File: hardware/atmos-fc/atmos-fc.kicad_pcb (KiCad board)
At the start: 4 copper layers, 40 x 40 mm, 109 parts, among them J1 Conn_01x04, J2 JST-SH 8p, J3 USB_C_Receptacle_USB2.0_16P, J4 Conn_01x03, J5 Conn_01x06, J6 Conn_01x06, J7 Conn_01x02, Q1 BC817, SW1 SW_Push, U1 MAX25232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

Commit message: Initial commit
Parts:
- removed the G*** at (146.1, 111.3)
- added G***: LOGO, 0_logo:atmos-fc_arrow-logo, F.Cu at (146.0, 111.2)
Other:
- board text removed: "V0.1 | 01/2024"

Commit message: Improved layout
Added oversized holes for mounting silicone inserts and improved layout.
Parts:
- H1, H2, H3, H4: footprint MountingHole:MountingHole_3.2mm_M3 -> MountingHole:MountingHole_4.3mm_M4
- U5: value IIM42352 -> ICM-42688-P
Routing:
- net +BATT_P: track 132.3 -> 147.4 mm, vias 11 -> 14
- net +5V: track 188.4 -> 200.4 mm, vias 23 -> 32
- net /Connectors/BUZZER-: track 7.29 -> 11.5 mm
- net +3V3: track 193.9 -> 192.4 mm
- net /Connectors/UART4_RX_C: track 38.0 -> 37.4 mm
- net /Connectors/UART4_TX_C: track 37.9 -> 37.4 mm
- net /Connectors/I2C_SCK: track 24.6 -> 24.1 mm
- net /Connectors/+5V_USB: track 63.2 -> 62.7 mm
- net GND: vias 135 -> 148

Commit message: Add GYRO_1_EXTI Pin
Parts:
- moved R5 0.50 mm to (141.6, 108.7)
- moved R11 0.30 mm to (137.5, 108.7)
- moved R4 0.25 mm to (140.2, 108.7)
- moved R17 0.20 mm to (135.6, 108.9)
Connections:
- net /MCU/BUZZER_CTRL renamed /MCU/BUZZER_EN
- net /MCU/BUZZER_CTRL_B renamed /MCU/BUZZER_EN_B
- U3 pad 32: unconnected-(U3-PA10-Pad32) -> /IMU/IMU_INT
- U5 pad 4: unconnected-(U5-INT1/INT-Pad4) -> /IMU/IMU_INT
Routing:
- net /IMU/IMU_INT: track 0.00 -> 11.9 mm, vias 0 -> 2
- net /IMU/IMU_SPI_MISO: track 7.66 -> 8.86 mm, vias 2 -> 0
- net /MCU/BUZZER_EN: track 11.7 -> 12.6 mm
- net /Connectors/I2C_SCK: track 24.1 -> 25.0 mm
- net /Connectors/I2C_SDA: track 21.8 -> 22.7 mm
- net /IMU/IMU_SPI_~{CS}: track 16.6 -> 17.4 mm
- net +3V3: track 192.4 -> 191.6 mm
- net /IMU/IMU_SPI_SCK: track 11.3 -> 11.9 mm
- net /Connectors/UART3_RX: track 19.9 -> 20.2 mm, vias 3 -> 2

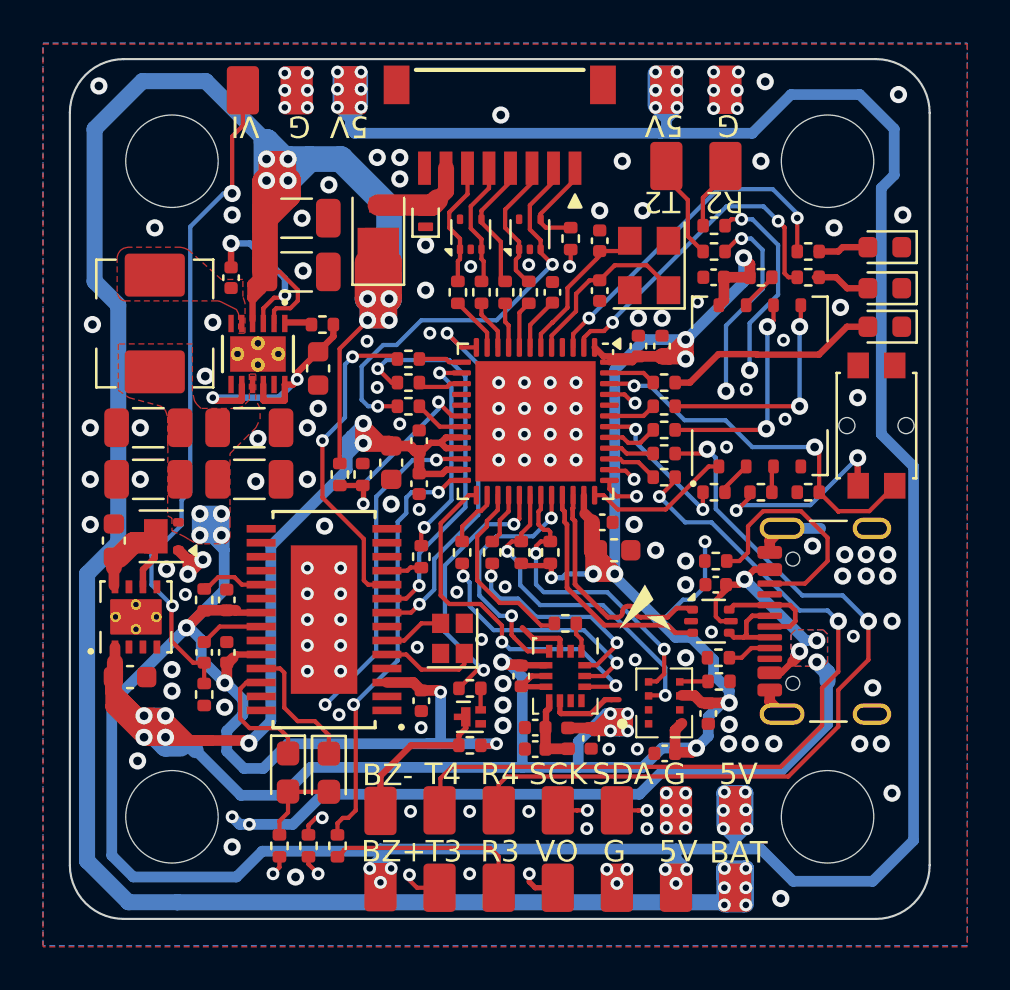
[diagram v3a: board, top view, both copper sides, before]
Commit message: Add soldering pads for ESC
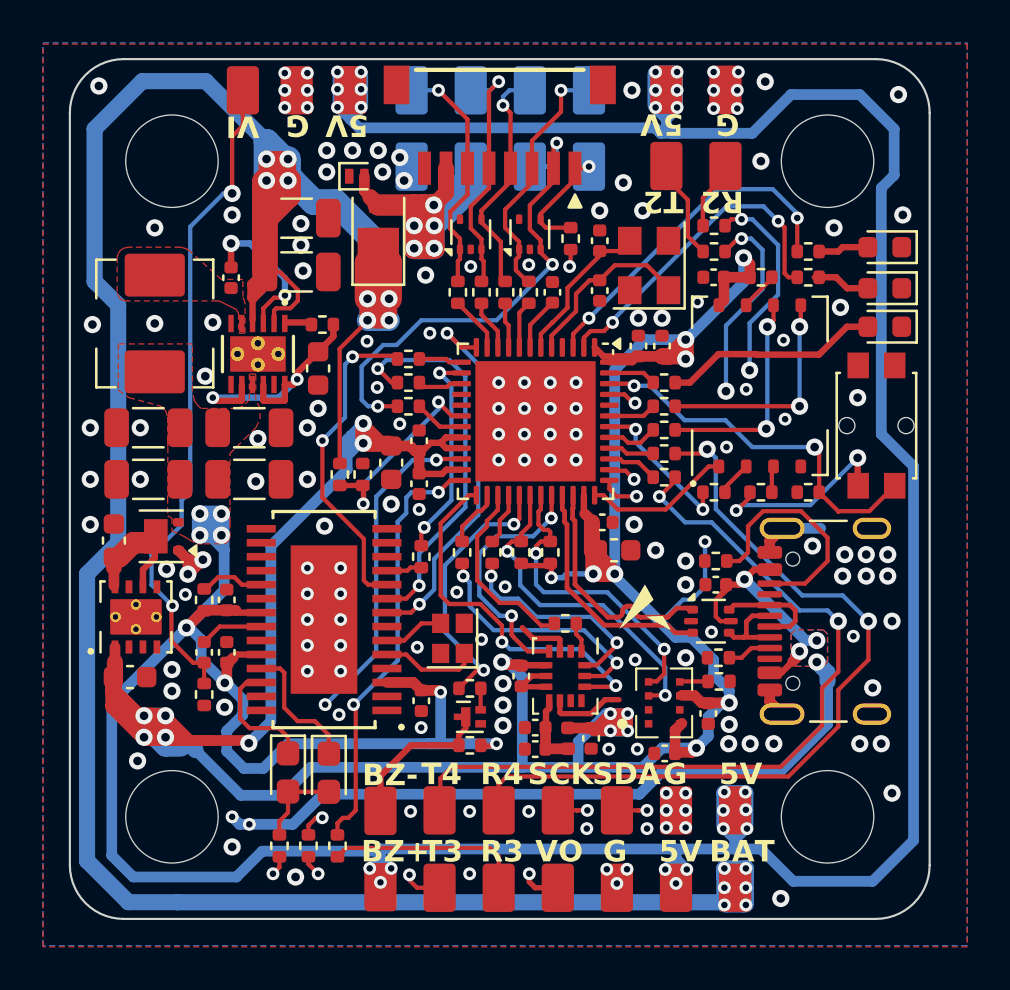
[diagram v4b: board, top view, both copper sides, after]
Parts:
- added J8: Conn_01x08, 0_connector:SolderWirePads-2x4, B.Cu at (139.3, 89.2)
- J1: footprint 0_connector:SolderWirePads-2x4 -> 0_connector:SolderWirePads-2x2
- moved G*** 25.2 mm to (121.8, 105.7), turned to 90 degrees
- moved D1 3.77 mm to (132.6, 91.2), turned to 0 degrees
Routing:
- net /Connectors/+BATT: track 4.49 -> 28.8 mm, vias 0 -> 5
- net +BATT_P: track 147.4 -> 140.1 mm
- net /Connectors/MOTOR2_C: track 5.77 -> 11.4 mm, vias 0 -> 1
- net /Connectors/MOTOR4_C: track 6.41 -> 11.9 mm, vias 0 -> 1
- net /Connectors/MOTOR1_C: track 5.87 -> 11.3 mm, vias 0 -> 1
- net /Connectors/MOTOR3_C: track 6.28 -> 11.1 mm, vias 0 -> 1
- net /Connectors/CURRENT_SENSE_C: track 19.5 -> 22.9 mm, vias 2 -> 3
- net /Connectors/TELEMETRY_C: track 4.69 -> 5.37 mm, vias 0 -> 1
- net GND: vias 148 -> 152
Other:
- board text added: "CURR"
- board text added: "M1"
- board text added: "M2"
- board text added: "M3"
- board text added: "M4"
- board text added: "RX"

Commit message: Added 100n on ADC inputs and improved layout
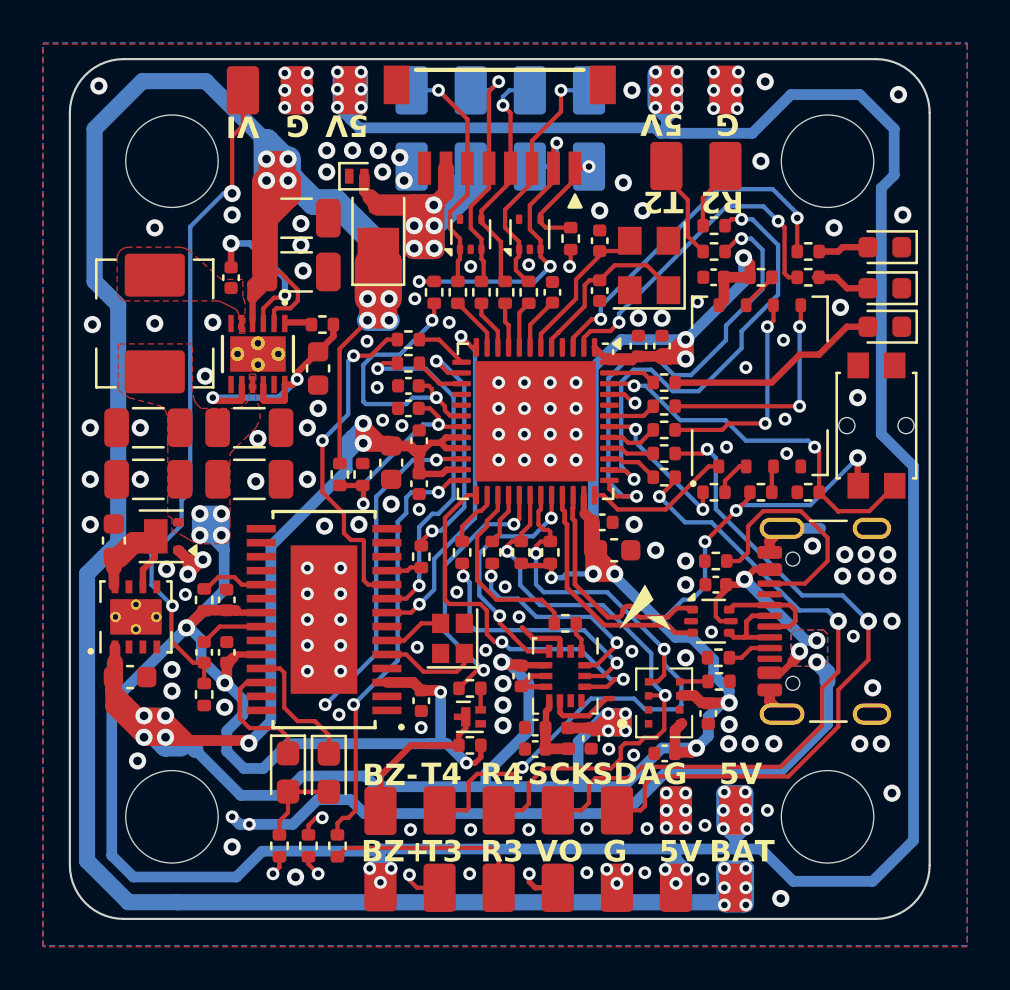
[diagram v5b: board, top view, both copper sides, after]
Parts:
- added C35: 100n, Capacitor_SMD:C_0402_1005Metric, F.Cu at (135.0, 102.0)
- added C36: 100n, Capacitor_SMD:C_0402_1005Metric, F.Cu at (135.0, 101.0)
- moved R31 5.43 mm to (136.2, 96.6), turned to 90 degrees
- moved R2 0.90 mm to (135.0, 98.8)
- moved R3 0.90 mm to (135.0, 99.9)
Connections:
- J5 pad 3: /Connectors/I2C_SDA -> /Connectors/UART4_RX_C
- J5 pad 4: /Connectors/I2C_SCK -> /Connectors/UART4_TX_C
- J5 pad 5: /Connectors/UART4_RX_C -> /Connectors/I2C_SDA
- J5 pad 6: /Connectors/UART4_TX_C -> /Connectors/I2C_SCK
- U3 pad 18: /MCU/MCU_VBAT_SENSE -> /Connectors/CURRENT_SENSE
- U3 pad 19: /Connectors/CURRENT_SENSE -> /MCU/MCU_VBAT_SENSE
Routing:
- net /Connectors/CURRENT_SENSE: track 2.36 -> 13.0 mm, vias 0 -> 2
- net /Connectors/CURRENT_SENSE_C: track 22.9 -> 15.8 mm
- net /Connectors/I2C_SCK: track 25.0 -> 31.7 mm
- net /Connectors/UART4_TX_C: track 37.4 -> 31.5 mm
- net /Connectors/UART4_RX_C: track 37.4 -> 31.8 mm
- net +3V3: track 191.6 -> 197.0 mm
- net /Connectors/I2C_SDA: track 22.7 -> 27.3 mm, vias 3 -> 2
- net /Connectors/UART2_TX: track 17.9 -> 22.2 mm, vias 3 -> 2
- net /Connectors/UART2_RX: track 18.9 -> 21.8 mm, vias 3 -> 2
- net /MCU/OSD_SPI_MISO: track 9.67 -> 11.5 mm
- net /MCU/OSD_SPI_MOSI: track 18.1 -> 16.5 mm
- net /MCU/OSD_SPI_~{CS}: track 17.7 -> 16.4 mm
- net /IMU/IMU_SPI_~{CS}: track 17.4 -> 18.1 mm
- net /MCU/OSD_SPI_SCK: track 15.1 -> 15.7 mm
- net /MCU/MCU_VBAT_SENSE: track 9.54 -> 10.1 mm
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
